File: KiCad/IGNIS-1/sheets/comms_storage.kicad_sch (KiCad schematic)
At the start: 5 parts, among them J30 SMA_antena, U30 RFM95W_SX1276_433MHz, U31 microSD

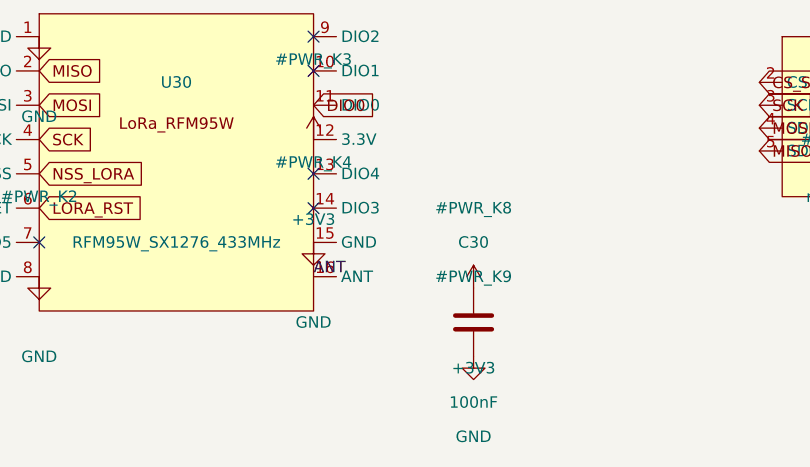
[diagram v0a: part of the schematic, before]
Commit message: Actualizado los boards de IGNIS - separado en 3 boards
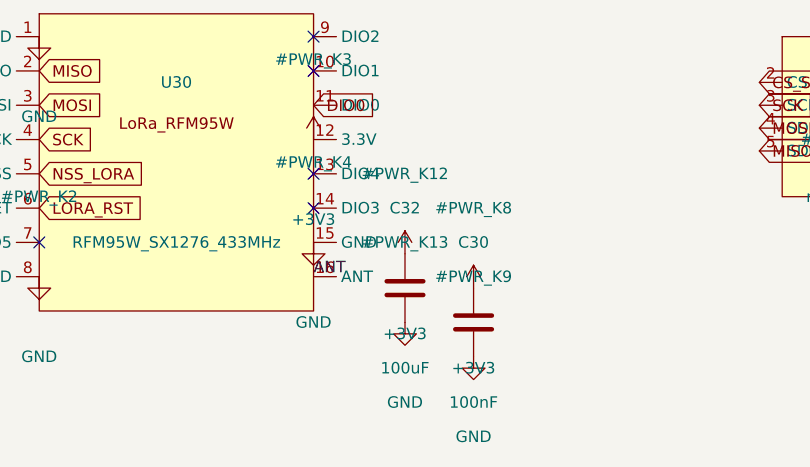
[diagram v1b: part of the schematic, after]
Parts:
- added C32: 100uF, Capacitor_SMD:C_1210_3225Metric, symbol Device:C
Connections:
- net +3V3: now also C32.1
- net GND: now also C32.2
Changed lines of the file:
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@@
 		(instances
 			(project "IGNIS-1"
-				(path "/58726030-ca17-4402-bd88-69b3f1ff686d/335a8c32-32cf-4d9c-93b1-920149cbd8fc" (reference "U30") (unit 1))))
+				(path "/5d1facc0-7dac-40de-a8c6-d3ccfbbb88f2/ecc3c020-1a6d-452e-abb6-add214c77511" (reference "U30") (unit 1))))
 	)
 	(symbol
@@
 		(instances
 			(project "IGNIS-1"
-				(path "/58726030-ca17-4402-bd88-69b3f1ff686d/335a8c32-32cf-4d9c-93b1-920149cbd8fc" (reference "U31") (unit 1))))
+				(path "/5d1facc0-7dac-40de-a8c6-d3ccfbbb88f2/ecc3c020-1a6d-452e-abb6-add214c77511" (reference "U31") (unit 1))))
 	)
 	(symbol
@@
 		(instances
 			(project "IGNIS-1"
-				(path "/58726030-ca17-4402-bd88-69b3f1ff686d/335a8c32-32cf-4d9c-93b1-920149cbd8fc" (reference "J30") (unit 1))))
+				(path "/5d1facc0-7dac-40de-a8c6-d3ccfbbb88f2/ecc3c020-1a6d-452e-abb6-add214c77511" (reference "J30") (unit 1))))
 	)
 	(symbol
@@
 		(instances
 			(project "IGNIS-1"
-				(path "/58726030-ca17-4402-bd88-69b3f1ff686d/335a8c32-32cf-4d9c-93b1-920149cbd8fc" (reference "C30") (unit 1))))
+				(path "/5d1facc0-7dac-40de-a8c6-d3ccfbbb88f2/ecc3c020-1a6d-452e-abb6-add214c77511" (reference "C30") (unit 1))))
 	)
 	(symbol
@@
 		(instances
 			(project "IGNIS-1"
-				(path "/58726030-ca17-4402-bd88-69b3f1ff686d/335a8c32-32cf-4d9c-93b1-920149cbd8fc" (reference "C31") (unit 1))))
+				(path "/5d1facc0-7dac-40de-a8c6-d3ccfbbb88f2/ecc3c020-1a6d-452e-abb6-add214c77511" (reference "C31") (unit 1))))
+	)
+	(symbol
+		(lib_id "Device:C")
+		(at 88.9 113.03 0)
+		(unit 1)
+		(exclude_from_sim no)
+		(in_bom yes)
+		(on_board yes)
+		(dnp no)
+		(property "Reference" "C32" (at 88.9 104.14 0) (effects (font (size 1.27 1.27))))
+		(property "Value" "100uF" (at 88.9 121.92 0) (effects (font (size 1.27 1.27))))
+		(property "Footprint" "Capacitor_SMD:C_1210_3225Metric" (at 88.9 113.03 0) (effects (font (size 1.27 1.27)) (hide yes)))
+		(property "Datasheet" "~" (at 88.9 113.03 0) (effects (font (size 1.27 1.27)) (hide yes)))
+		(pin "1")
+		(pin "2")
+		(instances
+			(project "IGNIS-1"
+				(path "/5d1facc0-7dac-40de-a8c6-d3ccfbbb88f2/ecc3c020-1a6d-452e-abb6-add214c77511" (reference "C32") (unit 1))))
 	)
 	(symbol
@@
 		(instances
 			(project "IGNIS-1"
-				(path "/58726030-ca17-4402-bd88-69b3f1ff686d/335a8c32-32cf-4d9c-93b1-920149cbd8fc" (reference "#PWR_K1") (unit 1))))
+				(path "/5d1facc0-7dac-40de-a8c6-d3ccfbbb88f2/ecc3c020-1a6d-452e-abb6-add214c77511" (reference "#PWR_K1") (unit 1))))
 	)
 	(global_label "MISO" (shape input) (at 48.26 88.9 0) (fields_autoplaced yes) (effects (font (size 1.27 1.27)) (justify left)))
@@
 		(instances
 			(project "IGNIS-1"
-				(path "/58726030-ca17-4402-bd88-69b3f1ff686d/335a8c32-32cf-4d9c-93b1-920149cbd8fc" (reference "#PWR_K2") (unit 1))))
+				(path "/5d1facc0-7dac-40de-a8c6-d3ccfbbb88f2/ecc3c020-1a6d-452e-abb6-add214c77511" (reference "#PWR_K2") (unit 1))))
 	)
 	(no_connect (at 78.74 85.09))
@@
 		(instances
 			(project "IGNIS-1"
-				(path "/58726030-ca17-4402-bd88-69b3f1ff686d/335a8c32-32cf-4d9c-93b1-920149cbd8fc" (reference "#PWR_K3") (unit 1))))
+				(path "/5d1facc0-7dac-40de-a8c6-d3ccfbbb88f2/ecc3c020-1a6d-452e-abb6-add214c77511" (reference "#PWR_K3") (unit 1))))
 	)
 	(no_connect (at 78.74 100.33))
@@
 		(instances
 			(project "IGNIS-1"
-				(path "/58726030-ca17-4402-bd88-69b3f1ff686d/335a8c32-32cf-4d9c-93b1-920149cbd8fc" (reference "#PWR_K4") (unit 1))))
+				(path "/5d1facc0-7dac-40de-a8c6-d3ccfbbb88f2/ecc3c020-1a6d-452e-abb6-add214c77511" (reference "#PWR_K4") (unit 1))))
 	)
 	(label "ANT" (at 78.74 111.76 0) (effects (font (size 1.27 1.27)) (justify left bottom)))
@@
 		(instances
 			(project "IGNIS-1"
-				(path "/58726030-ca17-4402-bd88-69b3f1ff686d/335a8c32-32cf-4d9c-93b1-920149cbd8fc" (reference "#PWR_K5") (unit 1))))
+				(path "/5d1facc0-7dac-40de-a8c6-d3ccfbbb88f2/ecc3c020-1a6d-452e-abb6-add214c77511" (reference "#PWR_K5") (unit 1))))
 	)
 	(global_label "CS_SD" (shape input) (at 128.26999999999998 90.17 0) (fields_autoplaced yes) (effects (font (size 1.27 1.27)) (justify left)))
@@
 		(instances
 			(project "IGNIS-1"
-				(path "/58726030-ca17-4402-bd88-69b3f1ff686d/335a8c32-32cf-4d9c-93b1-920149cbd8fc" (reference "#PWR_K6") (unit 1))))
+				(path "/5d1facc0-7dac-40de-a8c6-d3ccfbbb88f2/ecc3c020-1a6d-452e-abb6-add214c77511" (reference "#PWR_K6") (unit 1))))
 	)
 	(label "ANT" (at 25.4 71.12 0) (effects (font (size 1.27 1.27)) (justify left bottom)))
@@
 		(instances
 			(project "IGNIS-1"
-				(path "/58726030-ca17-4402-bd88-69b3f1ff686d/335a8c32-32cf-4d9c-93b1-920149cbd8fc" (reference "#PWR_K7") (unit 1))))
+				(path "/5d1facc0-7dac-40de-a8c6-d3ccfbbb88f2/ecc3c020-1a6d-452e-abb6-add214c77511" (reference "#PWR_K7") (unit 1))))
 	)
 	(symbol
@@
 		(instances
 			(project "IGNIS-1"
-				(path "/58726030-ca17-4402-bd88-69b3f1ff686d/335a8c32-32cf-4d9c-93b1-920149cbd8fc" (reference "#PWR_K8") (unit 1))))
+				(path "/5d1facc0-7dac-40de-a8c6-d3ccfbbb88f2/ecc3c020-1a6d-452e-abb6-add214c77511" (reference "#PWR_K8") (unit 1))))
 	)
 	(symbol
@@
 		(instances
 			(project "IGNIS-1"
-				(path "/58726030-ca17-4402-bd88-69b3f1ff686d/335a8c32-32cf-4d9c-93b1-920149cbd8fc" (reference "#PWR_K9") (unit 1))))
+				(path "/5d1facc0-7dac-40de-a8c6-d3ccfbbb88f2/ecc3c020-1a6d-452e-abb6-add214c77511" (reference "#PWR_K9") (unit 1))))
 	)
 	(symbol
@@
 		(instances
 			(project "IGNIS-1"
-				(path "/58726030-ca17-4402-bd88-69b3f1ff686d/335a8c32-32cf-4d9c-93b1-920149cbd8fc" (reference "#PWR_K10") (unit 1))))
+				(path "/5d1facc0-7dac-40de-a8c6-d3ccfbbb88f2/ecc3c020-1a6d-452e-abb6-add214c77511" (reference "#PWR_K10") (unit 1))))
 	)
 	(symbol
@@
 		(instances
 			(project "IGNIS-1"
-				(path "/58726030-ca17-4402-bd88-69b3f1ff686d/335a8c32-32cf-4d9c-93b1-920149cbd8fc" (reference "#PWR_K11") (unit 1))))
+				(path "/5d1facc0-7dac-40de-a8c6-d3ccfbbb88f2/ecc3c020-1a6d-452e-abb6-add214c77511" (reference "#PWR_K11") (unit 1))))
+	)
+	(symbol
+		(lib_id "power:+3V3")
+		(at 88.9 109.22 0)
+		(unit 1)
+		(exclude_from_sim no)
+		(in_bom yes)
+		(on_board yes)
+		(dnp no)
+		(property "Reference" "#PWR_K12" (at 88.9 100.33 0) (effects (font (size 1.27 1.27))))
+		(property "Value" "+3V3" (at 88.9 118.11 0) (effects (font (size 1.27 1.27))))
+		(property "Footprint" "" (at 88.9 109.22 0) (effects (font (size 1.27 1.27)) (hide yes)))
+		(property "Datasheet" "~" (at 88.9 109.22 0) (effects (font (size 1.27 1.27)) (hide yes)))
+		(pin "1")
+		(instances
+			(project "IGNIS-1"
+				(path "/5d1facc0-7dac-40de-a8c6-d3ccfbbb88f2/ecc3c020-1a6d-452e-abb6-add214c77511" (reference "#PWR_K12") (unit 1))))
+	)
+	(symbol
+		(lib_id "power:GND")
+		(at 88.9 116.84 0)
+		(unit 1)
+		(exclude_from_sim no)
+		(in_bom yes)
+		(on_board yes)
+		(dnp no)
+		(property "Reference" "#PWR_K13" (at 88.9 107.95 0) (effects (font (size 1.27 1.27))))
+		(property "Value" "GND" (at 88.9 125.73 0) (effects (font (size 1.27 1.27))))
+		(property "Footprint" "" (at 88.9 116.84 0) (effects (font (size 1.27 1.27)) (hide yes)))
+		(property "Datasheet" "~" (at 88.9 116.84 0) (effects (font (size 1.27 1.27)) (hide yes)))
+		(pin "1")
+		(instances
+			(project "IGNIS-1"
+				(path "/5d1facc0-7dac-40de-a8c6-d3ccfbbb88f2/ecc3c020-1a6d-452e-abb6-add214c77511" (reference "#PWR_K13") (unit 1))))
 	)
 	(text "IGNIS-1 -- Comunicacion + Almacenamiento. SPI compartido (MISO tri-state). LoRa RFM95W 433MHz SMA." (at 25.4 38.1 0) (effects (font (size 1.5 1.5)) (justify left)))
